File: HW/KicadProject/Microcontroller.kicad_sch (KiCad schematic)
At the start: 10 parts, among them J3 Conn_02x05_Odd_Even, SW1 SW_SPST, U2 STM32L011D4Px

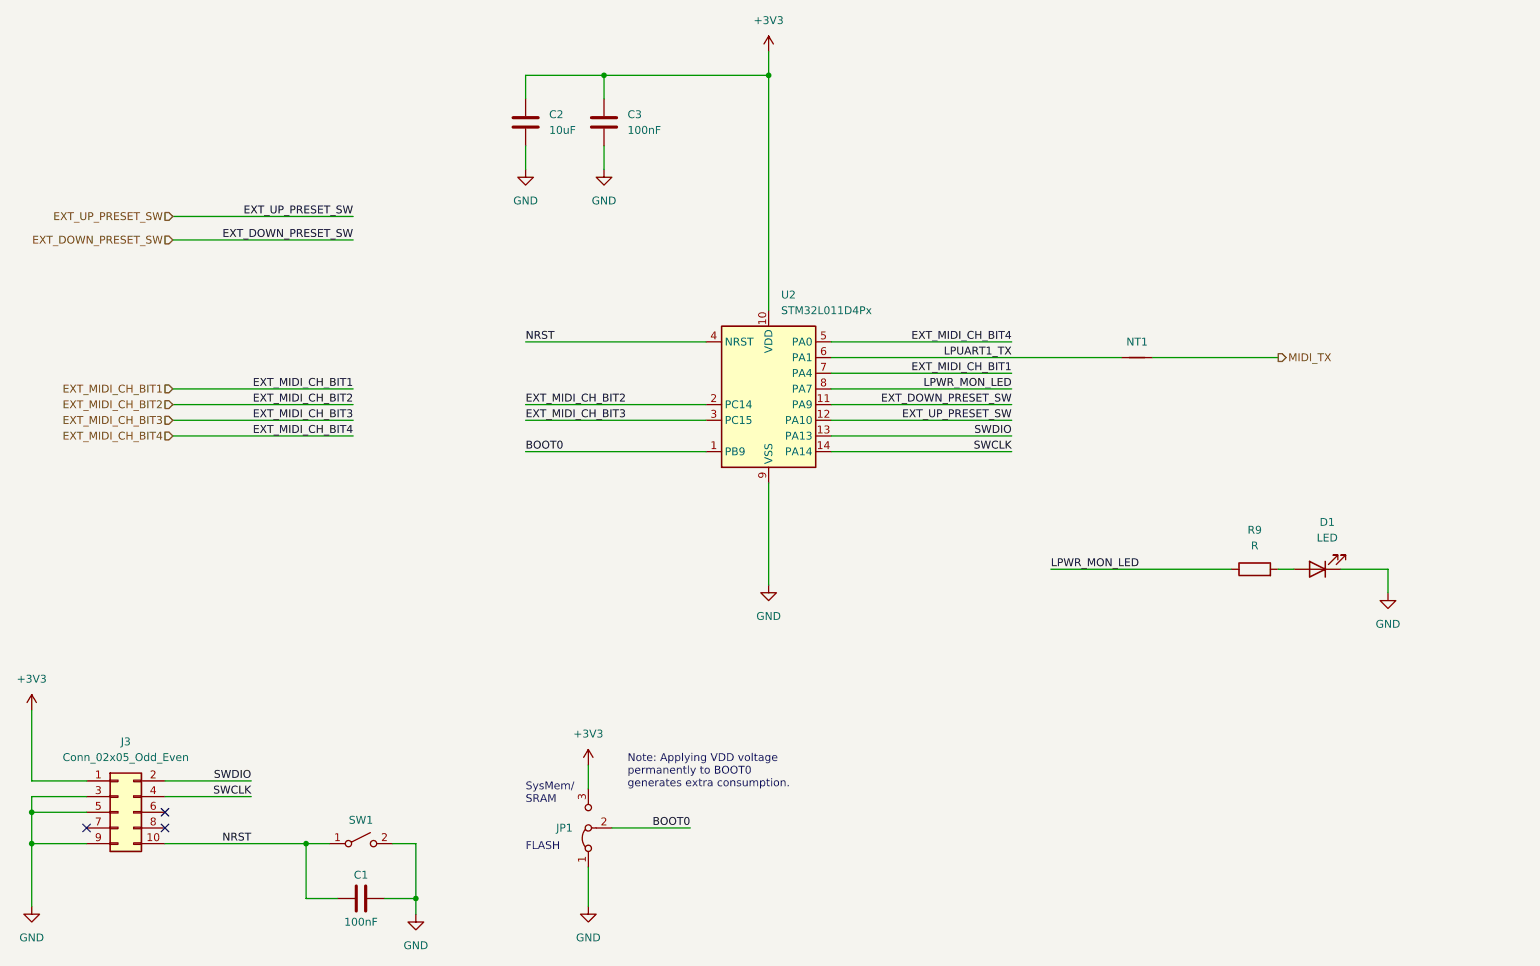
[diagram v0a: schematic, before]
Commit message: Updated to kicad 7.0.1, added stm32 doc links into schema page, regen pdf schema
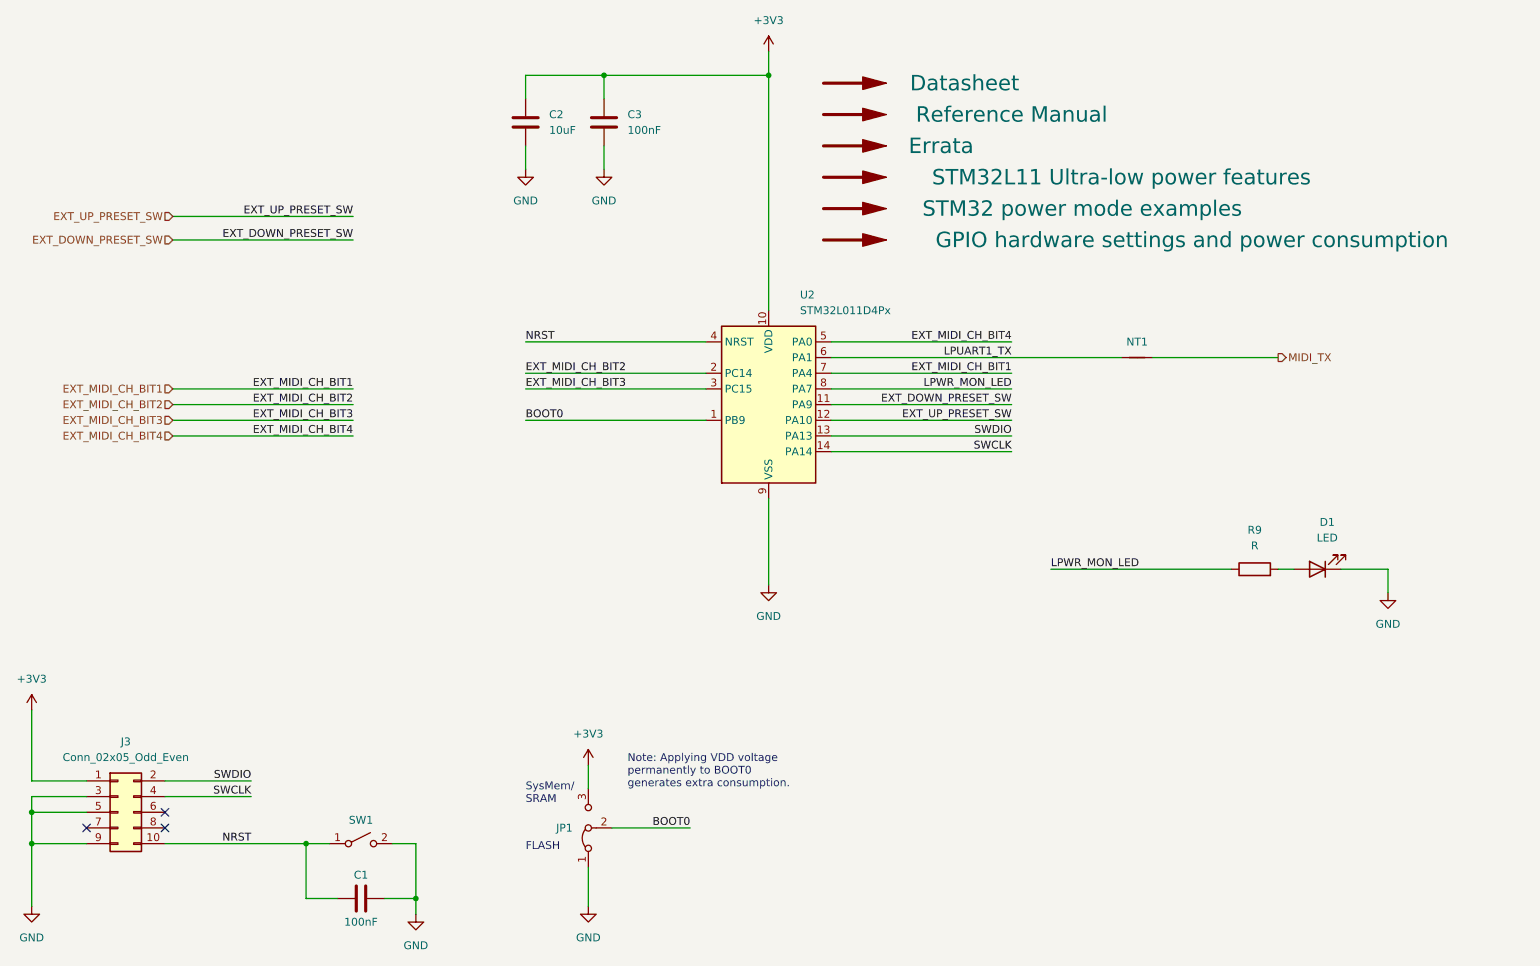
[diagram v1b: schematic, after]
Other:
- moved on the sheet: U2
